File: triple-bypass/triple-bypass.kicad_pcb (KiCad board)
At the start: 2 copper layers, 65 parts, among them CON101 MD-90SM, J101 HDR1X2, J102 HDR1X3, U101 THS7374IPWR, U102 LMV358M8G-13

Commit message: more parts placement
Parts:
- CON101: moved to B.Cu
- moved C113 58.4 mm to (128.6, 107.3), turned to 90 degrees
- moved YL 56.8 mm to (126.1, 128.0)
- moved C114 53.7 mm to (132.5, 107.2), turned to 90 degrees
- moved R107 52.0 mm to (139.7, 132.5)
- moved R108 52.0 mm to (143.5, 132.5)
- moved R109 52.0 mm to (147.3, 132.5)
- moved R110 52.0 mm to (151.1, 132.5)
- moved R112 51.8 mm to (148.8, 102.4), turned to 180 degrees
- moved R111 51.3 mm to (146.3, 110.6), turned to 180 degrees
- moved YR 49.5 mm to (136.0, 128.0)
- moved XL 48.4 mm to (129.4, 128.0)
- moved XR 47.7 mm to (132.7, 128.0)
- moved SN 44.3 mm to (131.1, 128.0)
- moved SL 42.5 mm to (127.8, 128.0)
- moved R106 40.8 mm to (143.9, 124.3), turned to 270 degrees
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- renumbered B1 to B, G1 to G, R1 to R, S1 to S, SL1 to SL, SN1 to SN, SL2 to SR, XL1 to XL, XL2 to XR, YL1 to YL, YL2 to YR

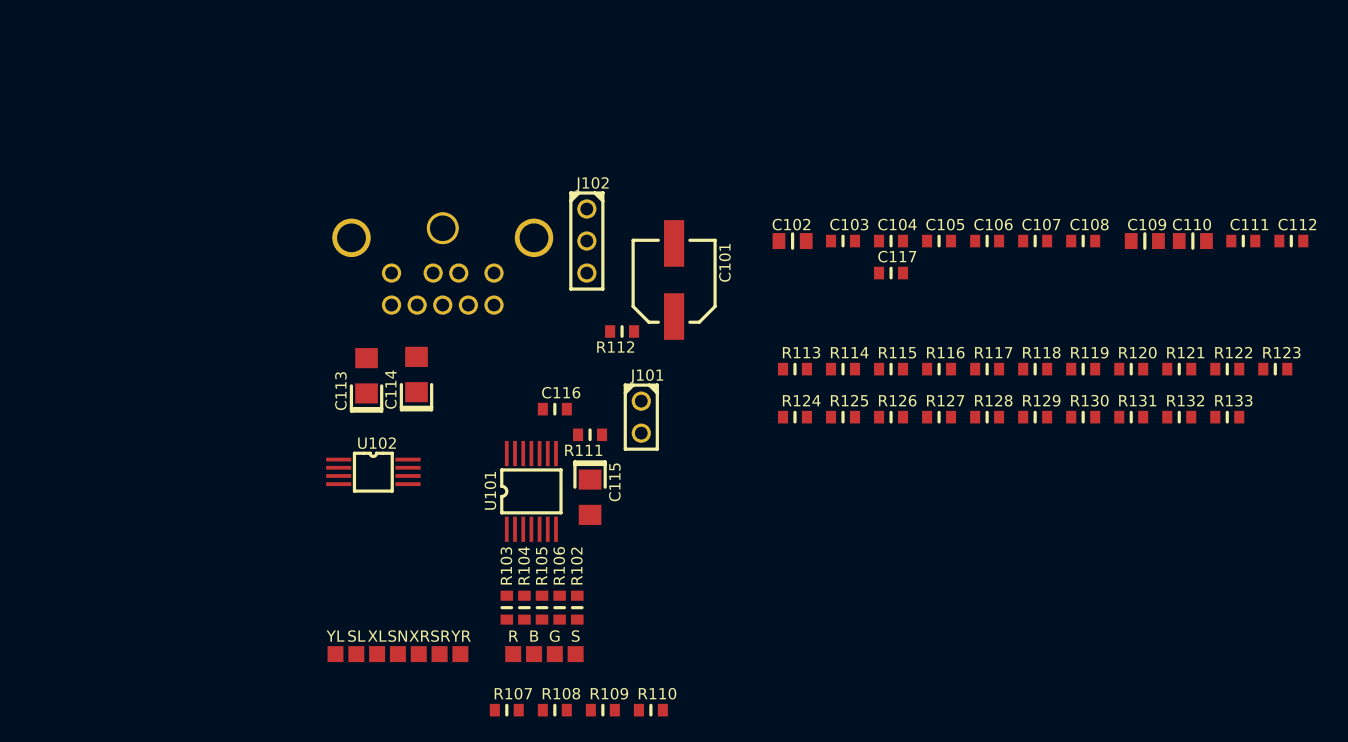
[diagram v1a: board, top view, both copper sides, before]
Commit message: v0.3 prelim routing complete, sch added
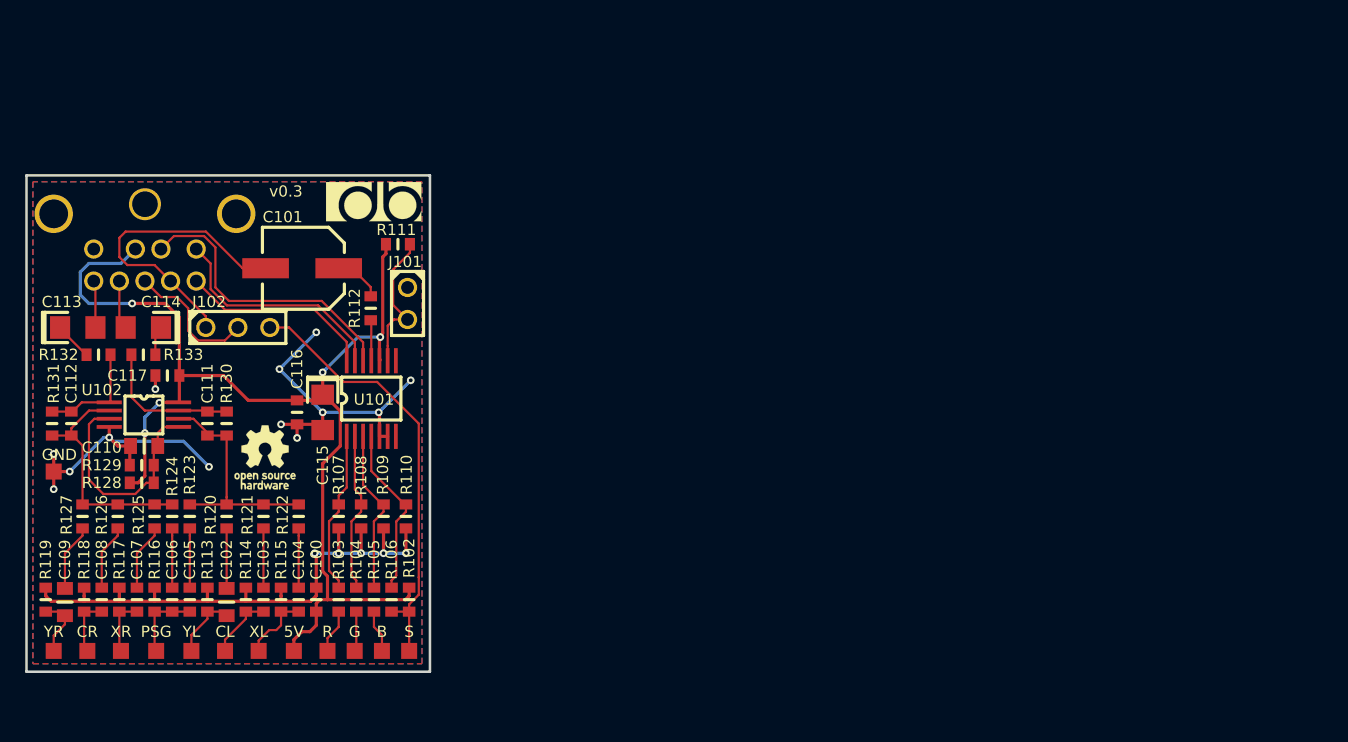
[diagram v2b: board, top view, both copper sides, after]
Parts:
- added 0V1: TP_50, db-smt:TP50, F.Cu at (103.8, 113.5)
- added 5V1: TP_50, db-smt:TP50, F.Cu at (122.8, 127.8)
- added C100: 0.1uF/50V, db-smt:0603, F.Cu at (124.6, 123.7)
- added G***: LOGO, db-artwork:oshw-logo_5mm, F.Cu at (120.5, 112.4)
- added G***: LOGO, db-artwork:db-logo_7.5mm, F.Cu at (129.2, 92.1)
- moved C112 97.9 mm to (105.2, 109.7), turned to 90 degrees
- moved C109 89.0 mm to (104.6, 122.8), turned to 270 degrees
- moved R123 86.9 mm to (114.6, 117.1), turned to 90 degrees
- moved R133 86.1 mm to (110.9, 104.3)
- moved R132 85.9 mm to (107.3, 104.3), turned to 180 degrees
- moved R131 85.6 mm to (103.6, 109.7), turned to 90 degrees
- moved C110 84.8 mm to (109.9, 111.5)
- moved R119 84.3 mm to (103.1, 123.7), turned to 90 degrees
- moved C111 83.4 mm to (116.0, 109.7), turned to 90 degrees
- moved C108 82.9 mm to (107.6, 123.7), turned to 90 degrees
- moved R118 77.6 mm to (106.2, 123.7), turned to 90 degrees
- moved C107 76.7 mm to (110.4, 123.7), turned to 90 degrees
- moved R122 74.6 mm to (123.2, 117.1), turned to 90 degrees
- moved R121 73.6 mm to (120.4, 117.1), turned to 90 degrees
- moved R120 72.7 mm to (117.5, 117.1), turned to 90 degrees
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- renumbered B to B1, G to G1, R to R1, S to S1, SL to SL1, SN to SN1, SR to SR2, XL to XL1, XR to XR2, YL to YL1, YR to YR2
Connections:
- net Net-(C102-Pad2) renamed /YM-Left
- net Net-(C103-Pad1) renamed /SCD-Left
- net Net-(C104-Pad1) renamed /32X-Left
- net Net-(C105-Pad1) renamed /PSG
- net Net-(C107-Pad1) renamed /32X-Right
- net Net-(C108-Pad1) renamed /SCD-Right
- net Net-(C109-Pad2) renamed /YM-Right
- net Net-(CON101-Pad1) renamed /B-Out
- net Net-(CON101-Pad3) renamed /G-Out
- net Net-(CON101-Pad7) renamed /R-Out
- net Net-(R1-Pad1) renamed /R-In
- B1 pad 1: Net-(B1-Pad1) -> /B-In
- G1 pad 1: Net-(G1-Pad1) -> /G-In
- R104 pad 2: Net-(B1-Pad1) -> /G-In
- R105 pad 2: Net-(G1-Pad1) -> /B-In
- U102 pad 1: Net-(C111-Pad2) -> Net-(C112-Pad2)
- U102 pad 2: Net-(C111-Pad1) -> Net-(C112-Pad1)
- U102 pad 6: Net-(C112-Pad1) -> Net-(C111-Pad1)
- U102 pad 7: Net-(C112-Pad2) -> Net-(C111-Pad2)
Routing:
- net GND: track 0.00 -> 95.8 mm, vias 0 -> 18
- net +5V: track 0.00 -> 91.7 mm, vias 0 -> 5
- net /SYNC-TTL: track 0.00 -> 34.7 mm
- net /SYNC-75: track 0.00 -> 24.2 mm
- net /B-Out: track 0.00 -> 23.3 mm
- net Net-(C111-Pad1): track 0.00 -> 19.1 mm
- net Net-(C112-Pad1): track 0.00 -> 18.8 mm
- net /G-Out: track 0.00 -> 18.3 mm
- net Net-(C110-Pad2): track 0.00 -> 18.1 mm
- net /R-Out: track 0.00 -> 15.4 mm
- net Net-(R106-Pad1): track 0.00 -> 13.7 mm
- net Net-(R105-Pad1): track 0.00 -> 13.1 mm
- net Net-(R103-Pad1): track 0.00 -> 12.9 mm
- net Net-(R104-Pad1): track 0.00 -> 12.7 mm
- net Net-(J101-Pad2): track 0.00 -> 11.5 mm
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- added copper zone on B.Cu, net GND
- added copper zone on F.Cu, net GND
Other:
- board outline added: 32 x 39.4 mm
- net class Default: clearance 0.2 -> 0.1778; trace_width 0.25 -> 0.1778; via_dia 0.6 -> 0.6096; via_drill 0.4 -> 0.3048
- net class Power added: clearance 0.1778, trace_width 0.254, via_dia 0.6096, via_drill 0.3048
- rule trace_clearance: 0.2 -> 0.1778
- rule trace_min: 0.2 -> 0.1778
- rule via_min_drill: 0.3 -> 0.3048
- rule via_min_size: 0.4 -> 0.6096
- board text added: "5V"
- board text added: "B"
- board text added: "CL"
- board text added: "CR"
- board text added: "G"
- board text added: "GND"
- board text added: "PSG"
- board text added: "R"
- board text added: "S"
- board text added: "XL"
- board text added: "XR"
- board text added: "YL"
- board text added: "YR"
- board text added: "v0.3"

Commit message: changed csync routing to pins 1/14 on 7374
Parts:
- J102: value HDR1X3 -> JMP-PCB-3POS; footprint db-thparts:HDR1X3 -> db-smt:JMP-PCB-3POS
- moved G*** 19.4 mm to (122.4, 93.1)
- moved R111 6.75 mm to (130.6, 102.2)
- moved S1 6.41 mm to (125.5, 127.8)
- moved J102 6.25 mm to (121.9, 100.7), turned to 0 degrees
- moved R112 5.84 mm to (124.8, 104.8), turned to 0 degrees
- moved R102 5.59 mm to (126.4, 123.7)
- moved R110 5.33 mm to (126.4, 117.1)
- moved C101 5.21 mm to (118.9, 102.4), turned to 270 degrees
- moved R130 4.97 mm to (116.6, 114.6), turned to 0 degrees
- moved C111 3.55 mm to (116.6, 113.2), turned to 0 degrees
- moved R104 2.79 mm to (130.6, 123.7)
- moved R105 2.79 mm to (132.0, 123.7)
- moved R106 2.79 mm to (127.8, 123.7)
- moved R103 2.79 mm to (129.2, 123.7)
- moved G1 2.16 mm to (129.8, 127.8)
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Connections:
- U101 pad 1: Net-(R103-Pad1) -> Net-(R106-Pad1)
- U101 pad 11: Net-(R112-Pad2) -> /B-Out
- U101 pad 12: /B-Out -> /G-Out
- U101 pad 13: /G-Out -> /R-Out
- U101 pad 14: /R-Out -> Net-(R112-Pad2)
- U101 pad 2: Net-(R104-Pad1) -> Net-(R103-Pad1)
- U101 pad 3: Net-(R105-Pad1) -> Net-(R104-Pad1)
- U101 pad 4: Net-(R106-Pad1) -> Net-(R105-Pad1)
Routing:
- net /SYNC-75: track 24.2 -> 10.9 mm
- net +5V: track 91.7 -> 84.1 mm, vias 5 -> 3
- net GND: track 95.8 -> 90.0 mm
- net /SYNC-OUT: track 10.8 -> 16.4 mm
- net Net-(J101-Pad2): track 11.5 -> 6.32 mm
- net Net-(C111-Pad2): track 11.4 -> 16.1 mm
- net Net-(C101-Pad1): track 3.89 -> 6.42 mm
- net Net-(R112-Pad2): track 3.23 -> 1.22 mm
- net /R-Out: track 15.4 -> 17.2 mm
- net Net-(C111-Pad1): track 19.1 -> 18.1 mm
- net Net-(R105-Pad1): track 13.1 -> 13.9 mm
- net Net-(R106-Pad1): track 13.7 -> 12.8 mm
- net Net-(R104-Pad1): track 12.7 -> 13.3 mm
- net /SYNC-TTL: track 34.7 -> 34.1 mm, vias 0 -> 2
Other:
- board text added: "db-electronics.ca"
- board text added: "triple bypass"

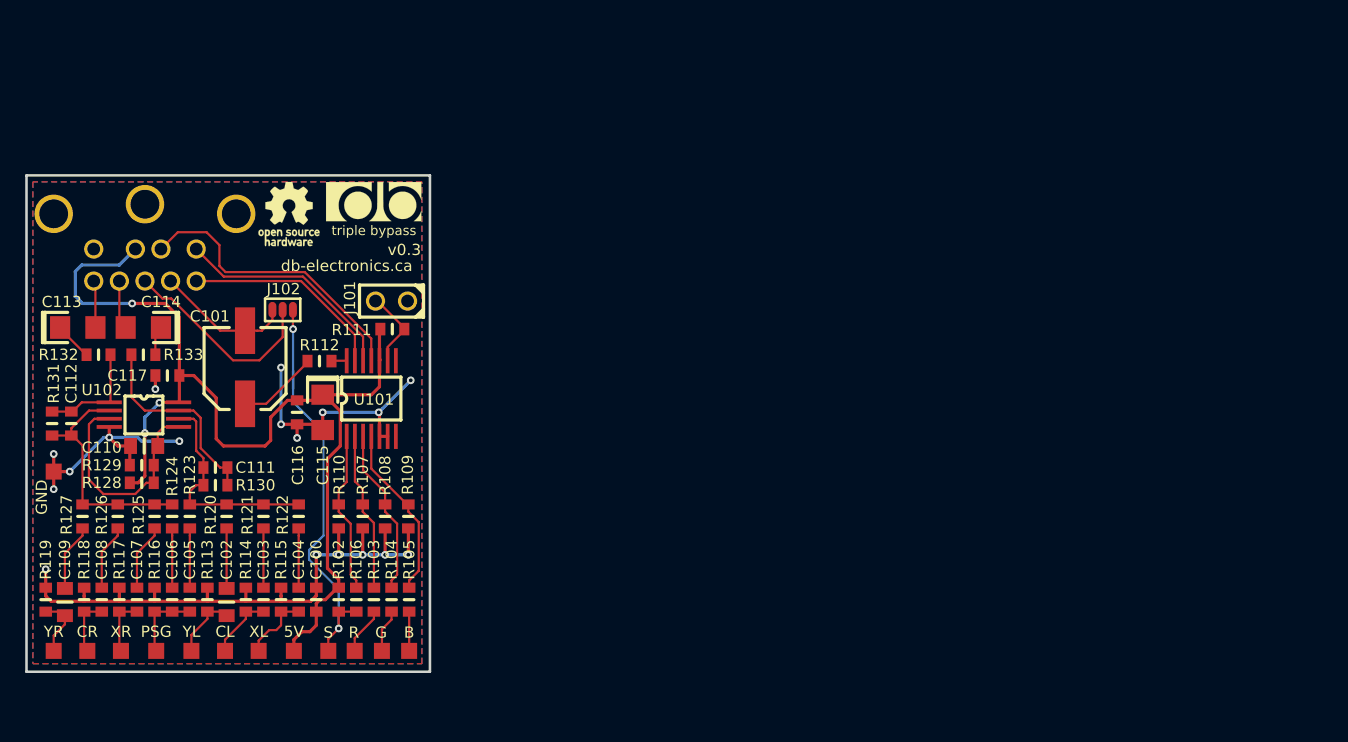
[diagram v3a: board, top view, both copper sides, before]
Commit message: Update to Mega Amp 2.0 and generated 3 seperated BOMs/SCH
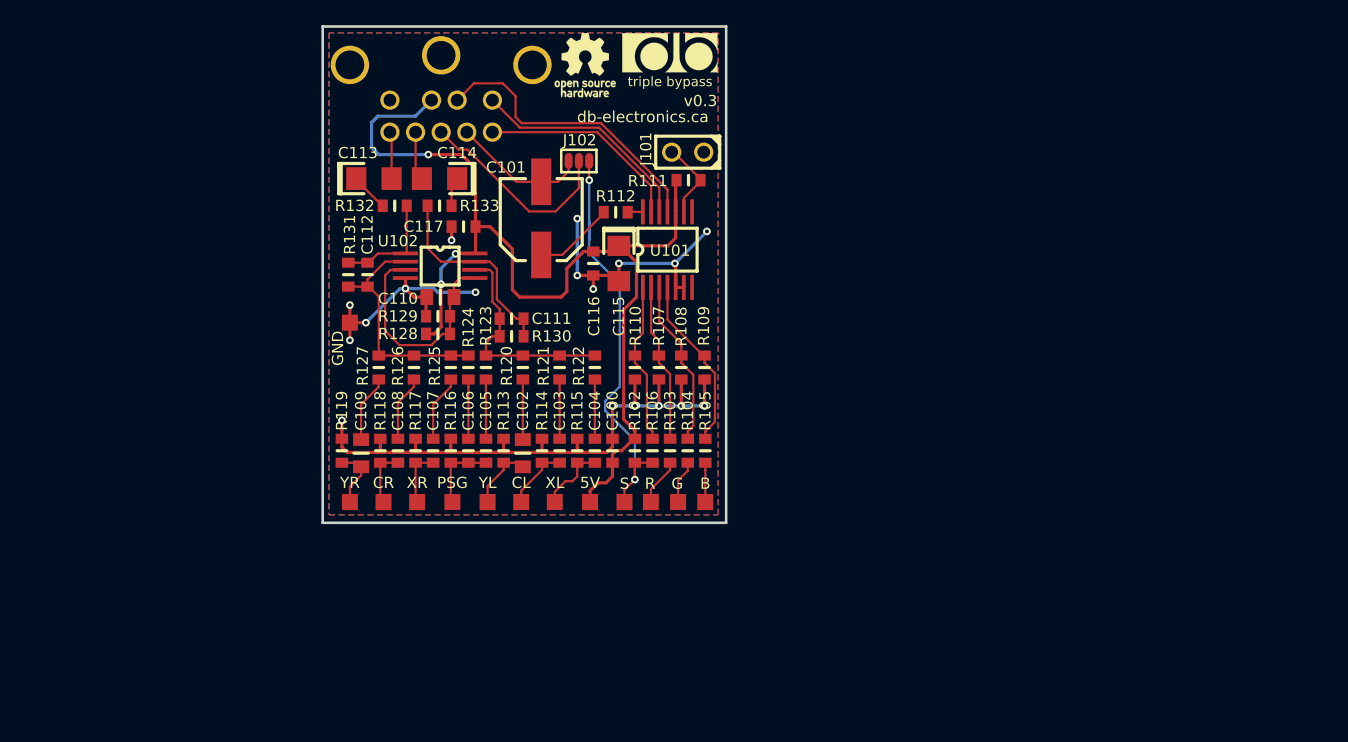
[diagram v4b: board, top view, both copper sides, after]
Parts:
- moved R112 26.3 mm to (148.3, 93.0)
- moved R102 26.3 mm to (149.9, 111.9)
- moved R110 26.3 mm to (149.9, 105.3)
- moved R117 26.3 mm to (132.5, 111.9)
- moved R133 26.3 mm to (134.4, 92.5)
- moved 5V1 26.3 mm to (146.3, 116.0)
- moved B1 26.3 mm to (155.4, 116.0)
- moved C113 26.3 mm to (127.8, 90.3)
- moved C114 26.3 mm to (135.8, 90.3)
- moved J101 26.3 mm to (155.3, 88.2)
- moved R128 26.3 mm to (134.2, 102.6)
- moved R129 26.3 mm to (134.2, 101.2)
- moved S1 26.3 mm to (149.0, 116.0)
- moved SN1 26.3 mm to (135.4, 116.0)
- moved YR2 26.3 mm to (127.3, 116.0)
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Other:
- board text added: "Licensed under CERN OHL v.1.2"
- board text added: "https://github.com/db-eletronics/ triple-bypass-kicad"
- board text added: "install MD-90SM on this side of PCB"
